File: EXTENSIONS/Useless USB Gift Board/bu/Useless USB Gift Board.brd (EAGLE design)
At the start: 19 x 40 mm, 6 parts, among them X1 USB-A

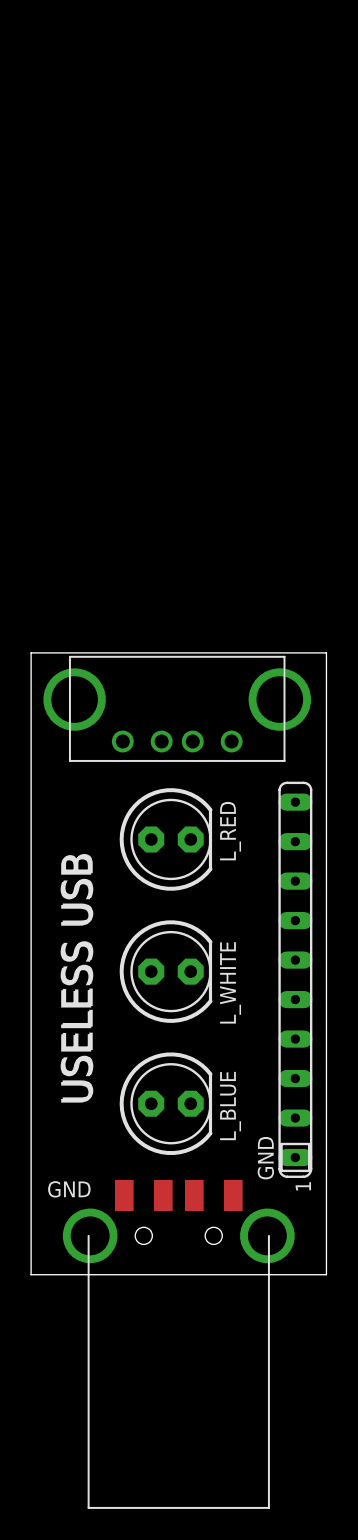
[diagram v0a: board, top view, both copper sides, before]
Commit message: Create v2 of Useless USB Gift Board, large board made by seeedstudio
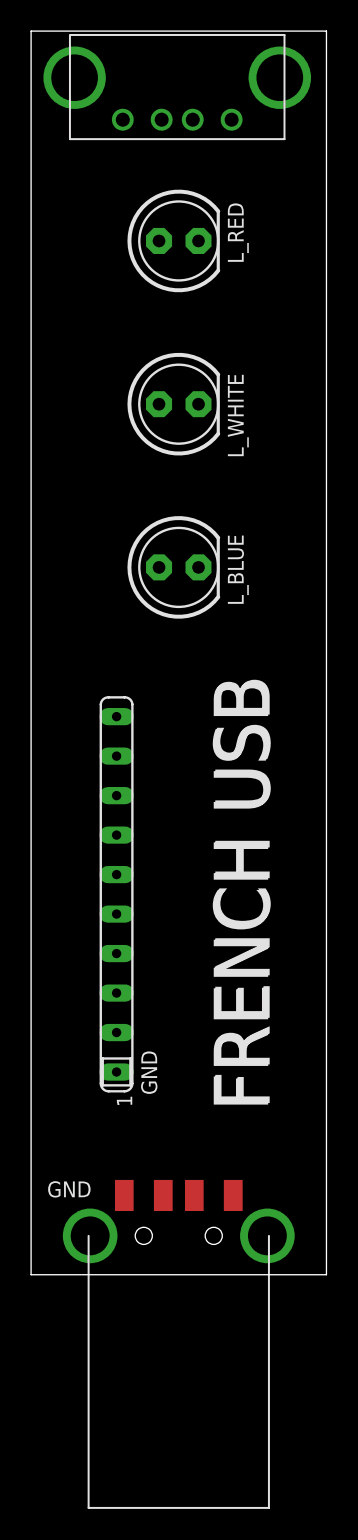
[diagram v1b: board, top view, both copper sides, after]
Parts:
- moved U$1 40.0 mm to (2.50, 73.0)
- moved L_RED 38.5 mm to (9.50, 66.5)
- moved L_WHITE 36.5 mm to (9.50, 56.0)
- moved L_BLUE 34.5 mm to (9.50, 45.5)
- moved RN1 12.7 mm to (5.50, 24.5)
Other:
- board size 19 x 40 mm -> 19 x 80 mm
- board text added: "FRENCH USB"
- board text added: "FredericTorres.com"
- board text added: "PCBv2 - 2019.09"
- board text removed: "Frederic Torres"
- board text removed: "PCBv1 - 2019.07"
- board text removed: "USELESS USB"
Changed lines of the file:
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@@
 <plain>
 <wire x1="0" y1="0" x2="19" y2="0" width="0" layer="20"/>
-<wire x1="19" y1="0" x2="19" y2="40" width="0" layer="20"/>
-<wire x1="19" y1="40" x2="0" y2="40" width="0" layer="20"/>
-<wire x1="0" y1="40" x2="0" y2="0" width="0" layer="20"/>
+<wire x1="19" y1="0" x2="19" y2="80" width="0" layer="20"/>
+<wire x1="19" y1="80" x2="0" y2="80" width="0" layer="20"/>
+<wire x1="0" y1="80" x2="0" y2="0" width="0" layer="20"/>
 <text x="3.9" y="6" size="1.016" layer="25" rot="R180">GND</text>
-<text x="14" y="19" size="1.016" layer="26" rot="MR270" align="center">PCBv1 - 2019.07</text>
-<text x="3" y="19" size="1.778" layer="26" rot="MR270" align="center">Frederic Torres</text>
-<text x="2.9" y="19" size="1.9304" layer="25" rot="R270" align="center">USELESS USB</text>
-<text x="15.1" y="7.5" size="1.016" layer="25" rot="R270" align="center">GND</text>
-<text x="3" y="19.1" size="1.9304" layer="25" rot="R270" align="center">USELESS USB</text>
+<text x="3" y="55" size="1.778" layer="26" rot="MR270" align="center">PCBv2 - 2019.09</text>
+<text x="16" y="38" size="3.81" layer="26" rot="MR270" align="center">FredericTorres.com</text>
+<text x="13.5" y="24.5" size="3.5" layer="25" rot="R270" align="center">FRENCH USB</text>
+<text x="7.6" y="13" size="1.016" layer="25" rot="R270" align="center">GND</text>
+<text x="13.6" y="24.6" size="3.5" layer="25" rot="R270" align="center">FRENCH USB</text>
 </plain>
 <attributes>
@@
 </autorouter>
 <elements>
-<element name="U$1" library="STUNTAZ" package="USB-FEMALE-A-PTH" value="USB" x="2.5" y="33" smashed="yes"/>
+<element name="U$1" library="STUNTAZ" package="USB-FEMALE-A-PTH" value="USB" x="2.5" y="73" smashed="yes"/>
 <element name="X1" library="adafruit" package="MOLEX_480371000" value="USB-A" x="9.5" y="2.5" smashed="yes"/>
-<element name="RN1" library="resistor-sip" package="SIP10" value="" x="17" y="19" smashed="yes" rot="R90">
-<attribute name="VALUE" x="15.23" y="23.92" size="1.27" layer="27" ratio="10" rot="R90"/>
-</element>
-<element name="L_BLUE" library="adafruit" package="LED5MM" value="" x="9" y="11" smashed="yes">
-<attribute name="NAME" x="13.175" y="8.5334" size="1.016" layer="25" ratio="10" rot="R90"/>
-<attribute name="VALUE" x="12.2004" y="9.1966" size="1.27" layer="27" ratio="10"/>
-</element>
-<element name="L_WHITE" library="adafruit" package="LED5MM" value="" x="9" y="19.5" smashed="yes">
-<attribute name="NAME" x="13.175" y="16.0334" size="1.016" layer="25" ratio="10" rot="R90"/>
-<attribute name="VALUE" x="12.2004" y="17.6966" size="1.27" layer="27" ratio="10"/>
-</element>
-<element name="L_RED" library="adafruit" package="LED5MM" value="" x="9" y="28" smashed="yes">
-<attribute name="NAME" x="13.175" y="26.5334" size="1.016" layer="25" ratio="10" rot="R90"/>
-<attribute name="VALUE" x="12.2004" y="26.1966" size="1.27" layer="27" ratio="10"/>
+<element name="RN1" library="resistor-sip" package="SIP10" value="" x="5.5" y="24.5" smashed="yes" rot="R90">
+<attribute name="VALUE" x="3.73" y="29.42" size="1.27" layer="27" ratio="10" rot="R90"/>
+</element>
+<element name="L_BLUE" library="adafruit" package="LED5MM" value="" x="9.5" y="45.5" smashed="yes">
+<attribute name="NAME" x="13.675" y="43.0334" size="1.016" layer="25" ratio="10" rot="R90"/>
+<attribute name="VALUE" x="12.7004" y="43.6966" size="1.27" layer="27" ratio="10"/>
+</element>
+<element name="L_WHITE" library="adafruit" package="LED5MM" value="" x="9.5" y="56" smashed="yes">
+<attribute name="NAME" x="13.675" y="52.5334" size="1.016" layer="25" ratio="10" rot="R90"/>
+<attribute name="VALUE" x="12.7004" y="54.1966" size="1.27" layer="27" ratio="10"/>
+</element>
+<element name="L_RED" library="adafruit" package="LED5MM" value="" x="9.5" y="66.5" smashed="yes">
+<attribute name="NAME" x="13.675" y="65.0334" size="1.016" layer="25" ratio="10" rot="R90"/>
+<attribute name="VALUE" x="12.7004" y="64.6966" size="1.27" layer="27" ratio="10"/>
 </element>
 </elements>
@@
 <contactref element="U$1" pad="GND"/>
 <contactref element="RN1" pad="1"/>
-<wire x1="17" y1="7.54" x2="5.9" y2="34.3" width="0" layer="19" extent="1-1"/>
-<wire x1="6" y1="5.1" x2="17" y2="7.54" width="0" layer="19" extent="1-1"/>
+<wire x1="5.5" y1="13.04" x2="5.9" y2="74.3" width="0" layer="19" extent="1-1"/>
+<wire x1="6" y1="5.1" x2="5.5" y2="13.04" width="0" layer="19" extent="1-1"/>
 </signal>
 <signal name="N$3">
 <contactref element="X1" pad="3"/>
 <contactref element="U$1" pad="D+"/>
-<wire x1="8.5" y1="5.1" x2="8.4" y2="34.3" width="0" layer="19" extent="1-1"/>
+<wire x1="8.5" y1="5.1" x2="8.4" y2="74.3" width="0" layer="19" extent="1-1"/>
 </signal>
 <signal name="N$4">
 <contactref element="X1" pad="2"/>
 <contactref element="U$1" pad="D-"/>
-<wire x1="10.5" y1="5.1" x2="10.4" y2="34.3" width="0" layer="19" extent="1-1"/>
+<wire x1="10.5" y1="5.1" x2="10.4" y2="74.3" width="0" layer="19" extent="1-1"/>
 </signal>
 <signal name="VCC">
@@
 <contactref element="L_WHITE" pad="A"/>
 <contactref element="L_RED" pad="A"/>
-<wire x1="7.73" y1="28" x2="12.9" y2="34.3" width="0" layer="19" extent="1-1"/>
-<wire x1="7.73" y1="19.5" x2="7.73" y2="28" width="0" layer="19" extent="1-1"/>
-<wire x1="7.73" y1="11" x2="7.73" y2="19.5" width="0" layer="19" extent="1-1"/>
-<wire x1="13" y1="5.1" x2="7.73" y2="11" width="0" layer="19" extent="1-1"/>
+<wire x1="8.23" y1="66.5" x2="12.9" y2="74.3" width="0" layer="19" extent="1-1"/>
+<wire x1="8.23" y1="56" x2="8.23" y2="66.5" width="0" layer="19" extent="1-1"/>
+<wire x1="8.23" y1="45.5" x2="8.23" y2="56" width="0" layer="19" extent="1-1"/>
+<wire x1="13" y1="5.1" x2="8.23" y2="45.5" width="0" layer="19" extent="1-1"/>
 </signal>
 <signal name="N$2">
 <contactref element="L_BLUE" pad="K"/>
 <contactref element="RN1" pad="2"/>
-<wire x1="10.27" y1="11" x2="17" y2="10.08" width="0" layer="19" extent="1-1"/>
+<wire x1="5.5" y1="15.58" x2="10.77" y2="45.5" width="0" layer="19" extent="1-1"/>
 </signal>
 <signal name="N$6">
 <contactref element="L_WHITE" pad="K"/>
 <contactref element="RN1" pad="6"/>
-<wire x1="10.27" y1="19.5" x2="17" y2="20.24" width="0" layer="19" extent="1-1"/>
+<wire x1="5.5" y1="25.74" x2="10.77" y2="56" width="0" layer="19" extent="1-1"/>
 </signal>
 <signal name="N$5">
 <contactref element="L_RED" pad="K"/>
 <contactref element="RN1" pad="8"/>
-<wire x1="17" y1="25.32" x2="10.27" y2="28" width="0" layer="19" extent="1-1"/>
+<wire x1="5.5" y1="30.82" x2="10.77" y2="66.5" width="0" layer="19" extent="1-1"/>
 </signal>
 </signals>
